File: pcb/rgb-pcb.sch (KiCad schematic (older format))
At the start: 35 parts, among them IC1 5V_REG, IC2 ATMEGA328P_TQFP, IC4 MAX3232, J1 SERIAL-POWER_out, J2 SERIAL-POWER_in, P1 AVR_ISP, P2 DEBUG, Y1 16MHz

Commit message: End of day commit
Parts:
- gave numbers to parts that had none: 1
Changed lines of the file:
@@
-EESchema Schematic File Version 2  date Mon 06 May 2013 12:04:28 PM CDT
+EESchema Schematic File Version 2  date Tue 07 May 2013 09:16:05 PM CDT
 LIBS:standard
 LIBS:avr-mcu
@@
 Sheet 1 1
 Title "diasy-chainable rgb lighting module"
-Date "5 may 2013"
+Date "8 may 2013"
 Rev "0.1"
 Comp "michael cousins - github.com/mcous"
@@
 	7350 1350 7350 1450
 $Comp
-L GND #PWR?
+L GND #PWR01
 U 1 1 5186F14D
 P 7400 4100
-F 0 "#PWR?" H 7400 4100 30  0001 C CNN
+F 0 "#PWR01" H 7400 4100 30  0001 C CNN
 F 1 "GND" H 7400 4030 30  0001 C CNN
 F 2 "" H 7400 4100 60  0001 C CNN
@@
 $EndComp
 $Comp
-L TLC5940_SOP IC?
+L TLC5940_SOP IC3
 U 1 1 5186F144
 P 7400 5200
-F 0 "IC?" H 7100 6100 60  0000 C CNN
+F 0 "IC3" H 7100 6100 60  0000 C CNN
 F 1 "TLC5940_SOP" H 7750 4300 60  0000 C CNN
 F 2 "" H 7400 5200 60  0001 C CNN
@@
 $EndComp
 $Comp
-L GND #PWR01
+L GND #PWR02
 U 1 1 5185A1C4
 P 7350 1750
-F 0 "#PWR01" H 7350 1750 30  0001 C CNN
+F 0 "#PWR02" H 7350 1750 30  0001 C CNN
 F 1 "GND" H 7350 1680 30  0001 C CNN
 F 2 "" H 7350 1750 60  0001 C CNN
@@
 V_BUS
 $Comp
-L C_POL C12
-U 1 1 5185A18C
-P 7350 1550
-F 0 "C12" V 7300 1700 60  0000 C CNN
-F 1 "10uF" V 7400 1750 60  0000 C CNN
-F 2 "" H 7350 1550 60  0001 C CNN
-F 3 "" H 7350 1550 60  0001 C CNN
-	1    7350 1550
-	0    1    1    0
-$EndComp
-$Comp
-L PWR_FLAG #FLG02
+L PWR_FLAG #FLG03
 U 1 1 5185A0FC
 P 2800 900
-F 0 "#FLG02" H 2800 995 30  0001 C CNN
+F 0 "#FLG03" H 2800 995 30  0001 C CNN
 F 1 "PWR_FLAG" H 2800 1080 30  0000 C CNN
 F 2 "" H 2800 900 60  0001 C CNN
@@
 NoConn ~ 9550 1550
 $Comp
-L GND #PWR03
+L GND #PWR04
 U 1 1 518598E3
 P 2800 1850
-F 0 "#PWR03" H 2800 1850 30  0001 C CNN
+F 0 "#PWR04" H 2800 1850 30  0001 C CNN
 F 1 "GND" H 2800 1780 30  0001 C CNN
 F 2 "" H 2800 1850 60  0001 C CNN
@@
 $EndComp
 $Comp
-L GND #PWR04
+L GND #PWR05
 U 1 1 51859848
 P 1850 2100
-F 0 "#PWR04" H 1850 2100 30  0001 C CNN
+F 0 "#PWR05" H 1850 2100 30  0001 C CNN
 F 1 "GND" H 1850 2030 30  0001 C CNN
 F 2 "" H 1850 2100 60  0001 C CNN
@@
 V_BUS
 $Comp
-L GND #PWR05
+L GND #PWR06
 U 1 1 51859815
 P 2150 1450
-F 0 "#PWR05" H 2150 1450 30  0001 C CNN
+F 0 "#PWR06" H 2150 1450 30  0001 C CNN
 F 1 "GND" H 2150 1380 30  0001 C CNN
 F 2 "" H 2150 1450 60  0001 C CNN
@@
 $EndComp
 $Comp
-L VCC #PWR06
+L VCC #PWR07
 U 1 1 51859808
 P 2900 1050
-F 0 "#PWR06" H 2900 1150 30  0001 C CNN
+F 0 "#PWR07" H 2900 1150 30  0001 C CNN
 F 1 "VCC" H 2900 1150 30  0000 C CNN
 F 2 "" H 2900 1050 60  0001 C CNN
@@
 $EndComp
 $Comp
-L GND #PWR07
+L GND #PWR08
 U 1 1 5185945E
 P 5350 3000
-F 0 "#PWR07" H 5350 3000 30  0001 C CNN
+F 0 "#PWR08" H 5350 3000 30  0001 C CNN
 F 1 "GND" H 5350 2930 30  0001 C CNN
 F 2 "" H 5350 3000 60  0001 C CNN
@@
 ADDR_0
 $Comp
-L VCC #PWR08
+L VCC #PWR09
 U 1 1 518593DD
 P 7050 2450
-F 0 "#PWR08" H 7050 2550 30  0001 C CNN
+F 0 "#PWR09" H 7050 2550 30  0001 C CNN
 F 1 "VCC" H 7050 2550 30  0000 C CNN
 F 2 "" H 7050 2450 60  0001 C CNN
@@
 NoConn ~ 9550 2000
 $Comp
-L GND #PWR09
+L GND #PWR010
 U 1 1 51858766
 P 10050 1450
-F 0 "#PWR09" H 10050 1450 30  0001 C CNN
+F 0 "#PWR010" H 10050 1450 30  0001 C CNN
 F 1 "GND" H 10050 1380 30  0001 C CNN
 F 2 "" H 10050 1450 60  0001 C CNN
@@
 $EndComp
 $Comp
-L VCC #PWR010
+L VCC #PWR011
 U 1 1 5185875E
 P 10050 1100
-F 0 "#PWR010" H 10050 1200 30  0001 C CNN
+F 0 "#PWR011" H 10050 1200 30  0001 C CNN
 F 1 "VCC" H 10050 1200 30  0000 C CNN
 F 2 "" H 10050 1100 60  0001 C CNN
@@
 $EndComp
 $Comp
-L VCC #PWR011
+L VCC #PWR012
 U 1 1 5185873E
 P 8450 1200
-F 0 "#PWR011" H 8450 1300 30  0001 C CNN
+F 0 "#PWR012" H 8450 1300 30  0001 C CNN
 F 1 "VCC" H 8450 1300 30  0000 C CNN
 F 2 "" H 8450 1200 60  0001 C CNN
@@
 $EndComp
 $Comp
-L GND #PWR012
+L GND #PWR013
 U 1 1 51858708
 P 8200 1600
-F 0 "#PWR012" H 8200 1600 30  0001 C CNN
+F 0 "#PWR013" H 8200 1600 30  0001 C CNN
 F 1 "GND" H 8200 1530 30  0001 C CNN
 F 2 "" H 8200 1600 60  0001 C CNN
@@
 RS_SLV_RX
 $Comp
-L GND #PWR013
+L GND #PWR014
 U 1 1 51858011
 P 6600 1600
-F 0 "#PWR013" H 6600 1600 30  0001 C CNN
+F 0 "#PWR014" H 6600 1600 30  0001 C CNN
 F 1 "GND" H 6600 1530 30  0001 C CNN
 F 2 "" H 6600 1600 60  0001 C CNN
@@
 V_BUS
 $Comp
-L GND #PWR014
+L GND #PWR015
 U 1 1 51858010
 P 6150 1100
-F 0 "#PWR014" H 6150 1100 30  0001 C CNN
+F 0 "#PWR015" H 6150 1100 30  0001 C CNN
 F 1 "GND" H 6150 1030 30  0001 C CNN
 F 2 "" H 6150 1100 60  0001 C CNN
@@
 $EndComp
 $Comp
-L PWR_FLAG #FLG015
+L PWR_FLAG #FLG016
 U 1 1 51857FF0
 P 1550 2200
-F 0 "#FLG015" H 1550 2295 30  0001 C CNN
+F 0 "#FLG016" H 1550 2295 30  0001 C CNN
 F 1 "PWR_FLAG" H 1550 2380 30  0000 C CNN
 F 2 "" H 1550 2200 60  0001 C CNN
@@
 $EndComp
 $Comp
-L PWR_FLAG #FLG016
+L PWR_FLAG #FLG017
 U 1 1 51857FD3
 P 1850 2200
-F 0 "#FLG016" H 1850 2295 30  0001 C CNN
+F 0 "#FLG017" H 1850 2295 30  0001 C CNN
 F 1 "PWR_FLAG" H 1850 2380 30  0000 C CNN
 F 2 "" H 1850 2200 60  0001 C CNN
@@
 $EndComp
 $Comp
-L GND #PWR017
+L GND #PWR018
 U 1 1 51857FA6
 P 4400 1100
-F 0 "#PWR017" H 4400 1100 30  0001 C CNN
+F 0 "#PWR018" H 4400 1100 30  0001 C CNN
 F 1 "GND" H 4400 1030 30  0001 C CNN
 F 2 "" H 4400 1100 60  0001 C CNN
@@
 V_BUS
 $Comp
-L GND #PWR018
+L GND #PWR019
 U 1 1 51857F67
 P 4850 1600
-F 0 "#PWR018" H 4850 1600 30  0001 C CNN
+F 0 "#PWR019" H 4850 1600 30  0001 C CNN
 F 1 "GND" H 4850 1530 30  0001 C CNN
 F 2 "" H 4850 1600 60  0001 C CNN
@@
 DC_MODE
 $Comp
-L VCC #PWR019
+L VCC #PWR020
 U 1 1 5181F756
 P 5850 5250
-F 0 "#PWR019" H 5850 5350 30  0001 C CNN
+F 0 "#PWR020" H 5850 5350 30  0001 C CNN
 F 1 "VCC" H 5850 5350 30  0000 C CNN
 F 2 "" H 5850 5250 60  0001 C CNN
@@
 SPI_MOSI
 $Comp
-L GND #PWR020
+L GND #PWR021
 U 1 1 5181EFE1
 P 4000 3150
-F 0 "#PWR020" H 4000 3150 30  0001 C CNN
+F 0 "#PWR021" H 4000 3150 30  0001 C CNN
 F 1 "GND" H 4000 3080 30  0001 C CNN
 F 2 "" H 4000 3150 60  0001 C CNN
@@
 $EndComp
 $Comp
-L VCC #PWR021
+L VCC #PWR022
 U 1 1 5181EFDA
 P 3950 2950
-F 0 "#PWR021" H 3950 3050 30  0001 C CNN
+F 0 "#PWR022" H 3950 3050 30  0001 C CNN
 F 1 "VCC" H 3950 3050 30  0000 C CNN
 F 2 "" H 3950 2950 60  0001 C CNN
@@
 $EndComp
 $Comp
-L GND #PWR022
+L GND #PWR023
 U 1 1 5181EFA2
 P 1650 4050
-F 0 "#PWR022" H 1650 4050 30  0001 C CNN
+F 0 "#PWR023" H 1650 4050 30  0001 C CNN
 F 1 "GND" H 1650 3980 30  0001 C CNN
 F 2 "" H 1650 4050 60  0001 C CNN
@@
 $EndComp
 $Comp
-L VCC #PWR023
+L VCC #PWR024
 U 1 1 5181EF92
 P 2200 3650
-F 0 "#PWR023" H 2200 3750 30  0001 C CNN
+F 0 "#PWR024" H 2200 3750 30  0001 C CNN
 F 1 "VCC" H 2200 3750 30  0000 C CNN
 F 2 "" H 2200 3650 60  0001 C CNN
@@
 $EndComp
 $Comp
-L GND #PWR024
+L GND #PWR025
 U 1 1 5181B718
 P 1650 5400
-F 0 "#PWR024" H 1650 5400 30  0001 C CNN
+F 0 "#PWR025" H 1650 5400 30  0001 C CNN
 F 1 "GND" H 1650 5330 30  0001 C CNN
 F 2 "" H 1650 5400 60  0001 C CNN
@@
 $EndComp
 $Comp
-L GND #PWR025
+L GND #PWR026
 U 1 1 5181B714
 P 1650 5200
-F 0 "#PWR025" H 1650 5200 30  0001 C CNN
+F 0 "#PWR026" H 1650 5200 30  0001 C CNN
 F 1 "GND" H 1650 5130 30  0001 C CNN
 F 2 "" H 1650 5200 60  0001 C CNN
@@
 $EndComp
 $Comp
-L GND #PWR026
+L GND #PWR027
 U 1 1 5181B47A
 P 2100 4300
-F 0 "#PWR026" H 2100 4300 30  0001 C CNN
+F 0 "#PWR027" H 2100 4300 30  0001 C CNN
 F 1 "GND" H 2100 4230 30  0001 C CNN
 F 2 "" H 2100 4300 60  0001 C CNN
@@
 $EndComp
 $Comp
-L VCC #PWR027
+L VCC #PWR028
 U 1 1 5181B46F
 P 2100 4750
-F 0 "#PWR027" H 2100 4850 30  0001 C CNN
+F 0 "#PWR028" H 2100 4850 30  0001 C CNN
 F 1 "VCC" H 2100 4850 30  0000 C CNN
 F 2 "" H 2100 4750 60  0001 C CNN
@@
 $EndComp
 $Comp
-L GND #PWR028
+L GND #PWR029
 U 1 1 5181AC1B
 P 6350 4750
-F 0 "#PWR028" H 6350 4750 30  0001 C CNN
+F 0 "#PWR029" H 6350 4750 30  0001 C CNN
 F 1 "GND" H 6350 4680 30  0001 C CNN
 F 2 "" H 6350 4750 60  0001 C CNN
@@
 $EndComp
 $Comp
-L VCC #PWR029
+L VCC #PWR030
 U 1 1 5181AC0E
 P 6400 4450
-F 0 "#PWR029" H 6400 4550 30  0001 C CNN
+F 0 "#PWR030" H 6400 4550 30  0001 C CNN
 F 1 "VCC" H 6400 4550 30  0000 C CNN
 F 2 "" H 6400 4450 60  0001 C CNN
@@
 	1    0    0    -1
 $EndComp
+$Comp
+L C_POL C12
+U 1 1 5189A717
+P 7350 1550
+F 0 "C12" V 7400 1700 60  0000 C CNN
+F 1 "10uF" V 7300 1750 60  0000 C CNN
+F 2 "" H 7350 1550 60  0000 C CNN
+F 3 "" H 7350 1550 60  0000 C CNN
+	1    7350 1550
+	0    1    1    0
+$EndComp
 $EndSCHEMATC

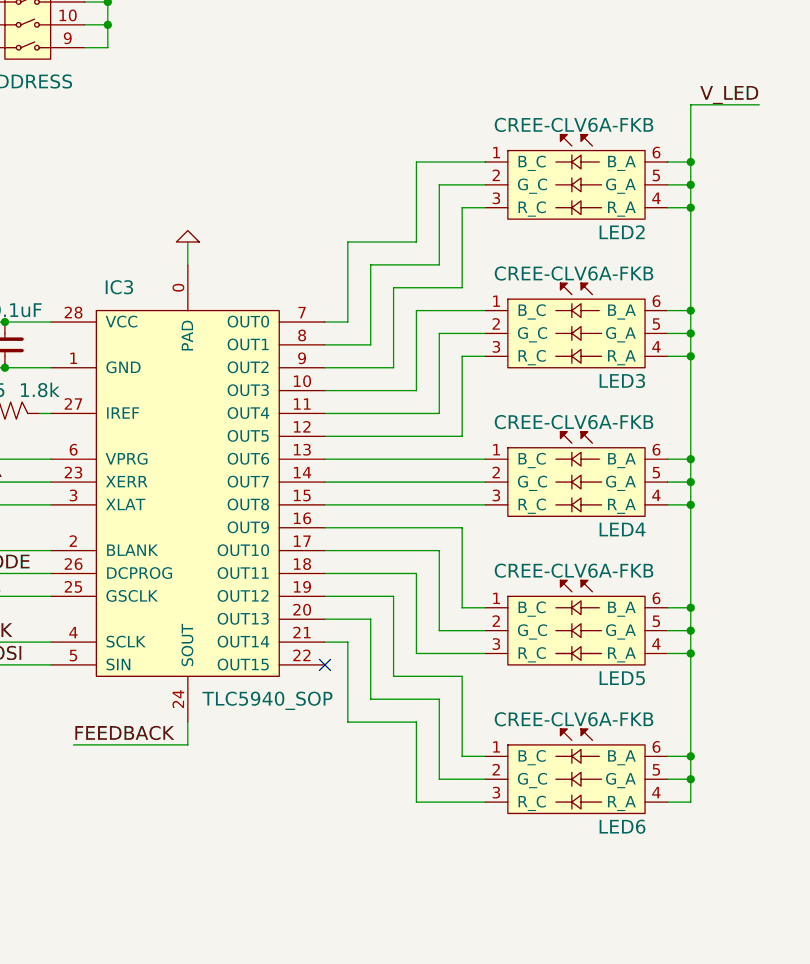
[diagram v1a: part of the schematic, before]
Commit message: Fixed up LED wiring and placed a majority of components. Board outline pretty set, running traces now
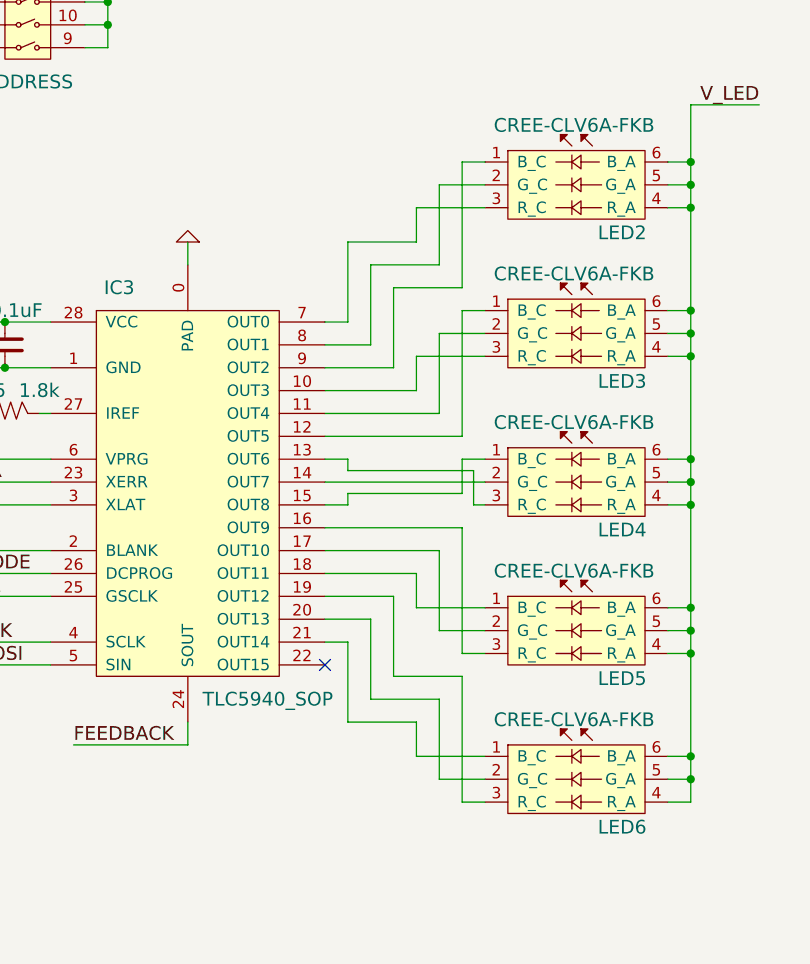
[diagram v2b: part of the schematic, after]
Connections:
- net at LED2.1 (B_C): now also IC3.9 (OUT2); no longer IC3.7 (OUT0)
- net at LED2.3 (R_C): now also IC3.7 (OUT0); no longer IC3.9 (OUT2)
- net at LED3.1 (B_C): now also IC3.12 (OUT5); no longer IC3.10 (OUT3)
- net at LED3.3 (R_C): now also IC3.10 (OUT3); no longer IC3.12 (OUT5)
- net at LED4.1 (B_C): now also IC3.15 (OUT8); no longer IC3.13 (OUT6)
- net at LED4.3 (R_C): now also IC3.13 (OUT6); no longer IC3.15 (OUT8)
- net at LED5.1 (B_C): now also IC3.18 (OUT11); no longer IC3.16 (OUT9)
- net at LED5.3 (R_C): now also IC3.16 (OUT9); no longer IC3.18 (OUT11)
- net at LED6.1 (B_C): now also IC3.21 (OUT14); no longer IC3.19 (OUT12)
- net at LED6.3 (R_C): now also IC3.19 (OUT12); no longer IC3.21 (OUT14)
